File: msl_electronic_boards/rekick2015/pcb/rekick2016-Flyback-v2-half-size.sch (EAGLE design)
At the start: 201 parts, among them IC1 74LVC1G02GW, IC2 4043D, IC3 LM1117, IC4 LM1458D, P1 39-30-06_S, P2 39-30-08_S, Q1 16MHz, Q2 IKW 25N120, Q3 PSMN7R8-120PS, Q5 IPD90P04P4L, Q6 IRF840, T1 BC859, T2 BC849, T3 BC849, T4 BC849, T5 IRLML6344TRPBF, T6 BC859, U1 TXB0108PWR, U3 LM2675, U4 LM2675, U5 ADUM4190BRIZ, U6 ADUM4190BRIZ, X1 87832-12, X2 87832-04

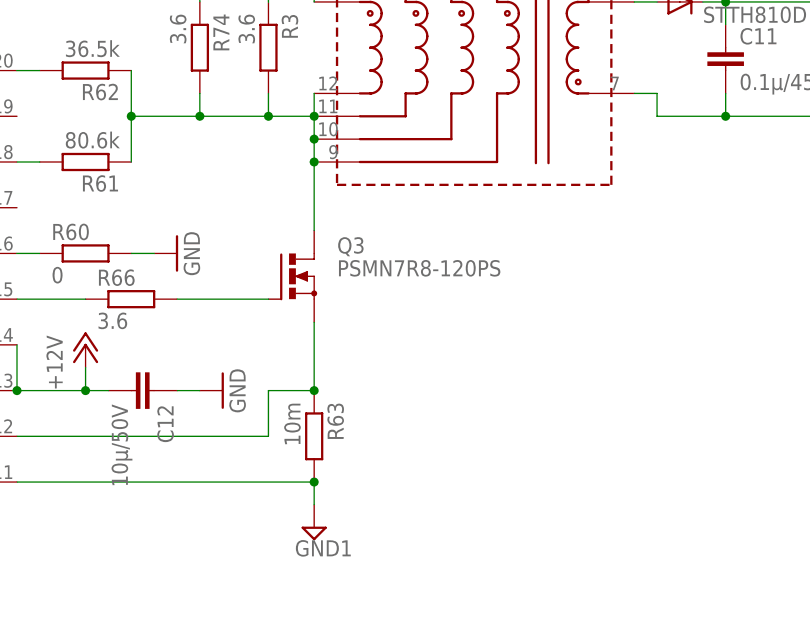
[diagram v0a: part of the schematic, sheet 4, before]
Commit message: rekick 2016 board for robocup workshop
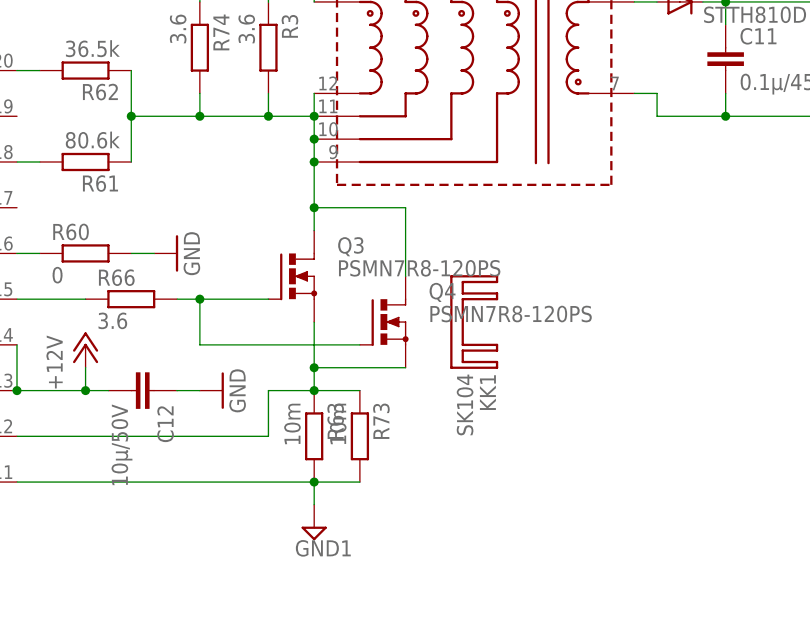
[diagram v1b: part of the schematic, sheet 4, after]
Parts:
- added KK1: SK104, heatsink:SK104
- added Q4: PSMN7R8-120PS, transistor-power:PMOSFET_NTO220BV
- added R73: 10m, R2818:R2818
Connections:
- net +12V: no longer R30.2
- net +24V: now also R30.2
- net GND1: now also R73.2
- net N$17: now also Q4.S, R73.1
- net N$18: now also Q4.G
- net N$24: now also Q4.D
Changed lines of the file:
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@@
 <part name="GND35" library="supply1" deviceset="GND" device=""/>
 <part name="SUPPLY30" library="supply2" deviceset="+5V/1" device=""/>
+<part name="P+17" library="supply1" deviceset="+24V" device=""/>
 <part name="C30" library="rcl" deviceset="C-EU" device="C1206" value="10µ/50V"/>
 <part name="C31" library="rcl" deviceset="C-EU" device="C1206" value="10µ/50V"/>
@@
 <part name="C49" library="rcl" deviceset="C-EU" device="C0603" value="100n"/>
 <part name="SUPPLY18" library="supply2" deviceset="+5V/3" device=""/>
+<part name="R73" library="R2818" deviceset="R2818" device="" value="10m"/>
+<part name="Q4" library="transistor-power" deviceset="PMOSFET_N" device="TO220BV" value="PSMN7R8-120PS"/>
+<part name="KK1" library="heatsink" deviceset="SK104" device=""/>
 <part name="R74" library="rcl" deviceset="R-EU_" device="R2010" value="3.6"/>
 <part name="C41" library="rcl" deviceset="C-EU" device="C1206" value="22n"/>
@@
 <part name="C29" library="rcl" deviceset="C-EU" device="C1206" value="10µ/50V"/>
 <part name="X2" library="con-molex" deviceset="87832-04" device=""/>
-<part name="P+17" library="supply1" deviceset="+12V" device=""/>
 </parts>
 <sheets>
@@
 <instance part="R67" gate="G$1" x="81.28" y="93.98"/>
 <instance part="R69" gate="G$1" x="58.42" y="60.96" rot="R180"/>
+<instance part="R73" gate="G$1" x="162.56" y="53.34" rot="R270"/>
+<instance part="Q4" gate="G$1" x="165.1" y="66.04"/>
+<instance part="KK1" gate="1" x="172.72" y="66.04" rot="R270"/>
 <instance part="R74" gate="G$1" x="144.78" y="96.52" rot="R270"/>
 <instance part="C41" gate="G$1" x="144.78" y="111.76"/>
@@
 <pinref part="U$9" gate="G$1" pin="CSN"/>
 <wire x1="157.48" y1="48.26" x2="124.46" y2="48.26" width="0.1524" layer="91"/>
+<pinref part="R73" gate="G$1" pin="2"/>
+<wire x1="162.56" y1="48.26" x2="157.48" y2="48.26" width="0.1524" layer="91"/>
 </segment>
 </net>
@@
 <pinref part="R63" gate="G$1" pin="1"/>
 <pinref part="Q3" gate="G$1" pin="S"/>
+<wire x1="157.48" y1="58.42" x2="157.48" y2="60.96" width="0.1524" layer="91"/>
 <pinref part="U$9" gate="G$1" pin="CSP"/>
-<wire x1="157.48" y1="58.42" x2="157.48" y2="66.04" width="0.1524" layer="91"/>
+<wire x1="157.48" y1="60.96" x2="157.48" y2="66.04" width="0.1524" layer="91"/>
 <wire x1="124.46" y1="53.34" x2="152.4" y2="53.34" width="0.1524" layer="91"/>
 <wire x1="152.4" y1="53.34" x2="152.4" y2="58.42" width="0.1524" layer="91"/>
 <wire x1="152.4" y1="58.42" x2="157.48" y2="58.42" width="0.1524" layer="91"/>
 <junction x="157.48" y="58.42"/>
+<pinref part="R73" gate="G$1" pin="1"/>
+<wire x1="157.48" y1="58.42" x2="162.56" y2="58.42" width="0.1524" layer="91"/>
+<pinref part="Q4" gate="G$1" pin="S"/>
+<wire x1="167.64" y1="60.96" x2="157.48" y2="60.96" width="0.1524" layer="91"/>
+<junction x="157.48" y="60.96"/>
 </segment>
 </net>
@@
 <pinref part="R66" gate="G$1" pin="2"/>
 <pinref part="Q3" gate="G$1" pin="G"/>
-<wire x1="142.24" y1="68.58" x2="152.4" y2="68.58" width="0.1524" layer="91"/>
+<wire x1="142.24" y1="68.58" x2="144.78" y2="68.58" width="0.1524" layer="91"/>
+<pinref part="Q4" gate="G$1" pin="G"/>
+<wire x1="144.78" y1="68.58" x2="152.4" y2="68.58" width="0.1524" layer="91"/>
+<wire x1="162.56" y1="63.5" x2="144.78" y2="63.5" width="0.1524" layer="91"/>
+<wire x1="144.78" y1="63.5" x2="144.78" y2="68.58" width="0.1524" layer="91"/>
+<junction x="144.78" y="68.58"/>
 </segment>
 </net>
@@
 <wire x1="157.48" y1="91.44" x2="157.48" y2="88.9" width="0.1524" layer="91"/>
 <pinref part="Q3" gate="G$1" pin="D"/>
-<wire x1="157.48" y1="83.82" x2="157.48" y2="76.2" width="0.1524" layer="91"/>
+<wire x1="157.48" y1="76.2" x2="157.48" y2="78.74" width="0.1524" layer="91"/>
+<pinref part="Q4" gate="G$1" pin="D"/>
+<wire x1="157.48" y1="78.74" x2="167.64" y2="78.74" width="0.1524" layer="91"/>
+<wire x1="167.64" y1="78.74" x2="167.64" y2="71.12" width="0.1524" layer="91"/>
+<wire x1="157.48" y1="83.82" x2="157.48" y2="78.74" width="0.1524" layer="91"/>
 <junction x="157.48" y="83.82"/>
+<junction x="157.48" y="78.74"/>
 <wire x1="144.78" y1="88.9" x2="152.4" y2="88.9" width="0.1524" layer="91"/>
 <junction x="144.78" y="88.9"/>
@@
 <instance part="GND37" gate="1" x="86.36" y="40.64"/>
 <instance part="C45" gate="G$1" x="246.38" y="157.48"/>
+<instance part="P+17" gate="1" x="187.96" y="172.72"/>
 <instance part="P+25" gate="1" x="81.28" y="25.4"/>
 <instance part="R58" gate="G$1" x="88.9" y="20.32" rot="R180"/>
@@
 <instance part="LED11" gate="G$1" x="142.24" y="38.1"/>
 <instance part="C37" gate="G$1" x="203.2" y="142.24"/>
-<instance part="P+17" gate="1" x="187.96" y="172.72"/>
 </instances>
 <busses>
@@
 <pinref part="U5" gate="A" pin="VDD1"/>
 </segment>
-<segment>
-<wire x1="187.96" y1="167.64" x2="187.96" y2="170.18" width="0.1524" layer="91"/>
-<pinref part="R30" gate="G$1" pin="2"/>
-<pinref part="P+17" gate="1" pin="+12V"/>
-</segment>
 </net>
 <net name="N$50" class="0">
@@
 </segment>
 </net>
+<net name="+24V" class="0">
+<segment>
+<wire x1="187.96" y1="167.64" x2="187.96" y2="170.18" width="0.1524" layer="91"/>
+<pinref part="R30" gate="G$1" pin="2"/>
+<pinref part="P+17" gate="1" pin="+24V"/>
+</segment>
+</net>
